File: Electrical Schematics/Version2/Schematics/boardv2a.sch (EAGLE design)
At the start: 562 parts, among them IC1 MCP41HVX1ST, IC2 ADUM4160BRW, IC3 SE555D, IC4 4030D, IC5 74LVC1G04DBV, IC6 74LVC1G04DBV, IC7 4030D, K1 G5V-2, Q1 IRLML2060TRPBFBSS123LT1G, Q10 IRLML2060TRPBFBSS123LT1G, Q11 IRLML2060TRPBFBSS123LT1G, Q13 IRLML2060TRPBFBSS123LT1G, Q14 IRLML2060TRPBFBSS123LT1G, Q15 IRLML2060TRPBFBSS123LT1G, Q16 IRLML2060TRPBFBSS123LT1G, Q17 IRLML2060TRPBFBSS123LT1G, Q18 BSP170P, Q19 IRLML2060TRPBFBSS123LT1G, Q2 IRLML2060TRPBFBSS123LT1G, Q3 IRLML2060TRPBFBSS123LT1G, Q4 BSP170P, Q5 IRLML2060TRPBFBSS123LT1G, Q6 IRLML2060TRPBFBSS123LT1G, Q7 ASFL1, Q8 IRLML2060TRPBFBSS123LT1G, Q9 IRLML2060TRPBFBSS123LT1G, U1 CP2130-GM, U10 SN65HVDA100-Q1_D_8, U11 ADUM3442CRWZ, U12 ADUM3442CRWZ, U13 ADUM3442CRWZ, U14 ADUM3442CRWZ, U15 ADUM3442CRWZ, U16 ADUM3442CRWZ, U17 ADUM3442CRWZ, U18 LM1085_KTT_3, U19 ADUM3442CRWZ, U2 TMS570LS0432_PZ_100, U20 ADUM3442CRWZ, U3 LM1085_KTT_3, U4 LM1085_KTT_3, U5 LM1084_KTT_3, U6 TPS3514_D_14, U7 LM1085_KTT_3, U9 ADUM3442CRWZ, X4 5566-4

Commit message: updarted board
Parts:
- removed IC4: 4030D, 40xx:4030D
- removed JP50: (no value), jumper:JP1Q
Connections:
- removed net CON_MOND_+: JP85.2
- removed net CON_MOND_-: C57.2
- removed net N$63: JP27.1
- new net FNR_CON_FD: D1.C, Q19.D, R14.2, TP149.TP
- new net FNR_CON_RD: D2.C, Q2.S, R15.2, TP148.TP
- net 5V_FNR: now also IC3.V+, IC7P.VDD, TP158.TP; no longer IC4P.VDD
- net CON_FNR_POTGND: now also TP160.TP
- net CON_MONA_+: now also JP85.2
- net CON_MONA_-: now also C57.2
- net CON_MONB_-: now also IC7P.VSS, TP159.TP; no longer IC4P.VSS
- net CON_RIN: now also JP27.1
- net FNR_CON_F: no longer D2.C, Q2.S, R15.2
- net FNR_CON_R: no longer D1.C, Q19.D, R14.2, TP149.TP
- net N$59: now also IC3.DIS
- net N$61: now also IC3.TR
- net N$62: now also IC3.Q
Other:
- moved on the sheet: C57, D1, JP27, JP85, PTC1, Q4, TP148, TP158, TP159, TP160

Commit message: updated stuff
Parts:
- removed TP143: TPB1,27, testpad:TPB1,27
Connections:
- new net 5V_SUP_J1: JP23.2, U$2.VSUP
- net 5V_SUPERVISED: no longer JP23.2, U$2.VSUP
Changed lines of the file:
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@@
 <part name="D3" library="diode" deviceset="GF1" device=""/>
 <part name="IC7" library="40xx" deviceset="4030" device="D"/>
-<part name="TP143" library="testpad" deviceset="TP" device="B1,27"/>
 <part name="TP144" library="testpad" deviceset="TP" device="B1,27"/>
 <part name="TP145" library="testpad" deviceset="TP" device="B1,27"/>
@@
 <net name="5V_SUPERVISED" class="0">
 <segment>
-<wire x1="50.8" y1="85.09" x2="52.07" y2="85.09" width="0.1524" layer="91"/>
-<wire x1="52.07" y1="85.09" x2="90.17" y2="85.09" width="0.1524" layer="91"/>
-<pinref part="U$2" gate="A" pin="VSUP"/>
-<junction x="52.07" y="85.09"/>
-<pinref part="JP23" gate="A" pin="2"/>
-<wire x1="90.17" y1="85.09" x2="90.17" y2="82.55" width="0.1524" layer="91"/>
-</segment>
-<segment>
 <pinref part="C9" gate="G$1" pin="1"/>
 <wire x1="97.79" y1="81.28" x2="110.49" y2="81.28" width="0.1524" layer="91"/>
@@
 </segment>
 </net>
+<net name="5V_SUP_J1" class="0">
+<segment>
+<wire x1="50.8" y1="85.09" x2="52.07" y2="85.09" width="0.1524" layer="91"/>
+<wire x1="52.07" y1="85.09" x2="90.17" y2="85.09" width="0.1524" layer="91"/>
+<pinref part="U$2" gate="A" pin="VSUP"/>
+<junction x="52.07" y="85.09"/>
+<pinref part="JP23" gate="A" pin="2"/>
+<wire x1="90.17" y1="85.09" x2="90.17" y2="82.55" width="0.1524" layer="91"/>
+</segment>
+</net>
 </nets>
 </sheet>
@@
 <instance part="IC5" gate="P" x="-71.12" y="22.86"/>
 <instance part="IC6" gate="P" x="-78.74" y="22.86"/>
-<instance part="TP143" gate="G$1" x="-17.78" y="76.2"/>
 <instance part="TP144" gate="G$1" x="-7.62" y="74.93"/>
 <instance part="TP145" gate="G$1" x="6.35" y="38.1"/>
@@
 <segment>
 <pinref part="D2" gate="D" pin="A"/>
-<label x="138.43" y="-41.91" size="1.778" layer="95" xref="yes"/>
-<wire x1="138.43" y1="-41.91" x2="119.38" y2="-40.64" width="0.1524" layer="91"/>
-<wire x1="137.16" y1="-36.83" x2="138.43" y2="-41.91" width="0.1524" layer="91"/>
+<label x="137.16" y="-40.64" size="1.778" layer="95" xref="yes"/>
+<wire x1="137.16" y1="-40.64" x2="119.38" y2="-40.64" width="0.1524" layer="91"/>
+<wire x1="137.16" y1="-36.83" x2="137.16" y2="-40.64" width="0.1524" layer="91"/>
 <pinref part="JP27" gate="A" pin="2"/>
 <wire x1="129.54" y1="-36.83" x2="137.16" y2="-36.83" width="0.1524" layer="91"/>
@@
 <junction x="41.91" y="76.2"/>
 </segment>
-<segment>
-<wire x1="39.37" y1="78.74" x2="40.64" y2="78.74" width="0.1524" layer="91"/>
-</segment>
 </net>

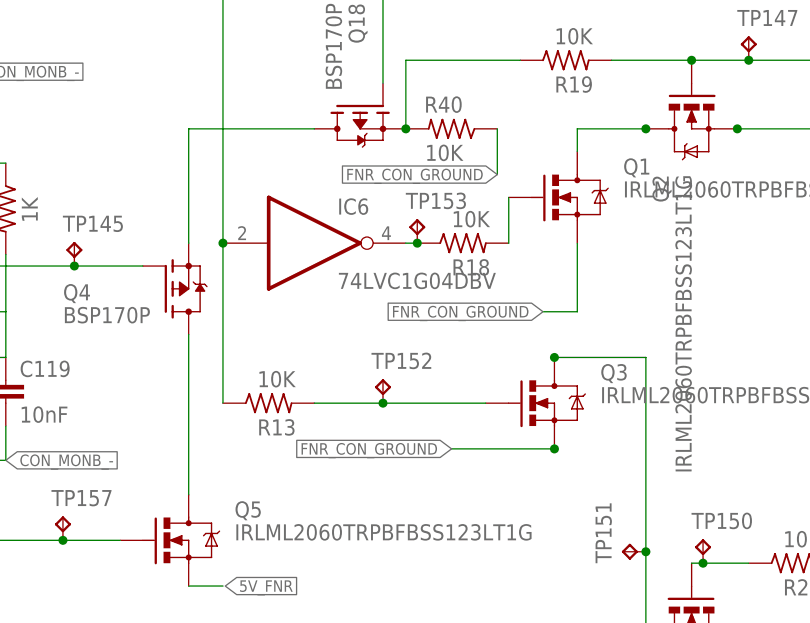
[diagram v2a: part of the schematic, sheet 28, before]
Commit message: fixed FNR ground
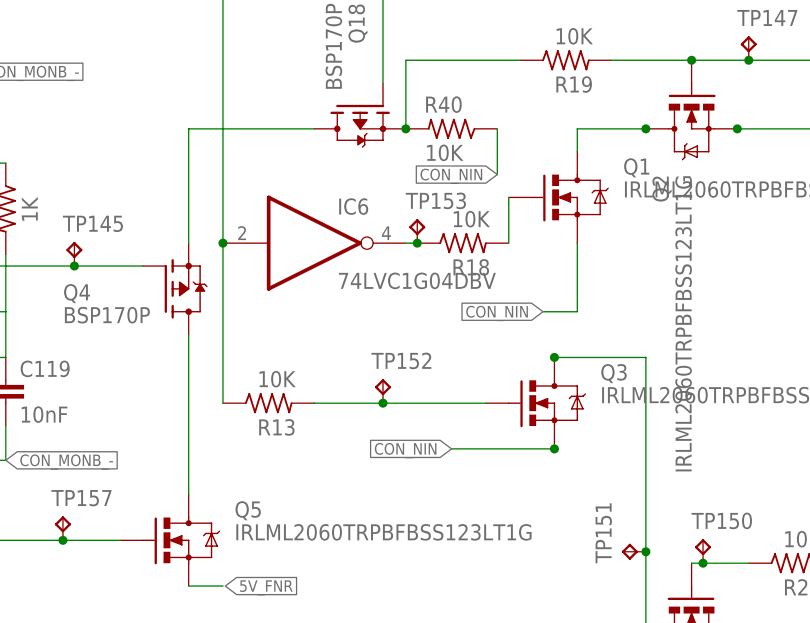
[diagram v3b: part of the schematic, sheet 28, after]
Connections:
- net CON_NIN: now also Q1.S, Q3.S, R40.1
- net FNR_CON_GROUND: no longer Q1.S, Q3.S, R40.1
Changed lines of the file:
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@@
 <setting verticaltext="up"/>
 </settings>
-<grid distance="0.05" unitdist="inch" unit="inch" style="lines" multiple="1" display="no" altdistance="0.025" altunitdist="inch" altunit="inch"/>
+<grid distance="0.1" unitdist="inch" unit="inch" style="lines" multiple="1" display="no" altdistance="0.01" altunitdist="inch" altunit="inch"/>
 <layers>
 <layer number="1" name="Top" color="4" fill="1" visible="no" active="no"/>
@@
 </segment>
 </net>
-<net name="FNR_CON_GROUND" class="0">
-<segment>
-<pinref part="Q3" gate="G$1" pin="S"/>
-<label x="48.26" y="15.24" size="1.27" layer="95" rot="R180" xref="yes"/>
-<wire x1="59.69" y1="15.24" x2="48.26" y2="15.24" width="0.1524" layer="91"/>
-<junction x="59.69" y="15.24"/>
-</segment>
-<segment>
-<wire x1="62.23" y1="38.1" x2="62.23" y2="30.48" width="0.1524" layer="91"/>
-<wire x1="62.23" y1="30.48" x2="58.42" y2="30.48" width="0.1524" layer="91"/>
-<label x="58.42" y="30.48" size="1.27" layer="95" rot="R180" xref="yes"/>
-<pinref part="Q1" gate="G$1" pin="S"/>
-</segment>
-<segment>
-<pinref part="R40" gate="G$1" pin="1"/>
-<wire x1="53.34" y1="50.8" x2="53.34" y2="45.72" width="0.1524" layer="91"/>
-<label x="53.34" y="45.72" size="1.27" layer="95" rot="R180" xref="yes"/>
-</segment>
-</net>
 <net name="FNR_CON_R" class="0">
 <segment>
@@
 <junction x="41.91" y="76.2"/>
 </segment>
+<segment>
+<pinref part="R40" gate="G$1" pin="1"/>
+<wire x1="53.34" y1="50.8" x2="53.34" y2="45.72" width="0.1524" layer="91"/>
+<label x="53.34" y="45.72" size="1.27" layer="95" rot="R180" xref="yes"/>
+</segment>
+<segment>
+<pinref part="Q3" gate="G$1" pin="S"/>
+<label x="48.26" y="15.24" size="1.27" layer="95" rot="R180" xref="yes"/>
+<wire x1="59.69" y1="15.24" x2="48.26" y2="15.24" width="0.1524" layer="91"/>
+<junction x="59.69" y="15.24"/>
+</segment>
+<segment>
+<wire x1="62.23" y1="38.1" x2="62.23" y2="30.48" width="0.1524" layer="91"/>
+<wire x1="62.23" y1="30.48" x2="58.42" y2="30.48" width="0.1524" layer="91"/>
+<label x="58.42" y="30.48" size="1.27" layer="95" rot="R180" xref="yes"/>
+<pinref part="Q1" gate="G$1" pin="S"/>
+</segment>
 </net>

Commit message: did some lagit routing
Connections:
- net MCU_COMMS_MISO: now also JP14.1
- net MCU_COMMS_SCK: now also JP18.2
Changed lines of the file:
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@@
 <junction x="114.3" y="-7.62"/>
 <wire x1="355.6" y1="-93.98" x2="355.6" y2="-86.36" width="0.1524" layer="91"/>
-<wire x1="355.6" y1="-86.36" x2="373.38" y2="-86.36" width="0.1524" layer="91"/>
+<wire x1="355.6" y1="-86.36" x2="370.84" y2="-86.36" width="0.1524" layer="91"/>
 <pinref part="JP13" gate="A" pin="2"/>
+<wire x1="370.84" y1="-86.36" x2="373.38" y2="-86.36" width="0.1524" layer="91"/>
 <wire x1="355.6" y1="-93.98" x2="375.92" y2="-93.98" width="0.1524" layer="91"/>
 <junction x="355.6" y="-93.98"/>
+<pinref part="JP14" gate="A" pin="1"/>
+<junction x="370.84" y="-86.36"/>
 </segment>
 </net>
@@
 <wire x1="375.92" y1="-116.84" x2="370.84" y2="-116.84" width="0.1524" layer="91"/>
 <wire x1="370.84" y1="-116.84" x2="370.84" y2="-121.92" width="0.1524" layer="91"/>
-<wire x1="370.84" y1="-121.92" x2="378.46" y2="-121.92" width="0.1524" layer="91"/>
+<wire x1="370.84" y1="-121.92" x2="375.92" y2="-121.92" width="0.1524" layer="91"/>
 <junction x="370.84" y="-116.84"/>
+<pinref part="JP18" gate="A" pin="2"/>
+<wire x1="375.92" y1="-121.92" x2="378.46" y2="-121.92" width="0.1524" layer="91"/>
+<junction x="375.92" y="-121.92"/>
 </segment>
 </net>

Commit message: Lots of routing and some lib updates
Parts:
- removed R22, R23: (no value), resistor-bourns:4816P-T01E
- removed TP117: TPB1,27, testpad:TPB1,27
- added U$32, U$4: RHM1620CT-ND, shit:RHM1620CT-ND
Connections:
- new net 5V_SU_J: JP25.2, U$3.VSUP
- new net N$301: JP80.8
- new net N$302: JP80.7
- net 5V_SUPERVISED: no longer JP25.2, U$3.VSUP
- net FPGA_MCU_AD1: now also U$4G$7.P$1; no longer R22B.1
- net FPGA_MCU_AD2: now also U$4G$6.P$1; no longer R22C.1
- net FPGA_MCU_AD3: now also U$4G$5.P$1; no longer R22D.1
- net FPGA_MCU_AD4: now also U$4G$4.P$1; no longer R22E.1
- net FPGA_MCU_AD5: now also U$4G$3.P$1; no longer R22F.1
- net FPGA_MCU_AD6: now also U$4G$2.P$1; no longer R22G.1
- net FPGA_MCU_AD7: now also U$4G$1.P$1; no longer R22H.1
- net FPGA_MCU_AD7_RES: now also U$4G$1.P$2; no longer R22H.2
- net FPGA_MCU_ADO: now also U$4G$8.P$1; no longer R22A.1
- net FPGA_MCU_RES1: now also U$32G$1.P$1; no longer R23A.1
- net FPGA_MCU_RES1_RES: now also U$32G$1.P$2; no longer R23A.2
- net FPGA_MCU_RES2: now also U$32G$2.P$1; no longer R23B.1
- net FPGA_MCU_RES2_RES: now also U$32G$2.P$2; no longer R23B.2
- net FPGA_MCU_RES3: now also U$32G$3.P$1; no longer R23C.1
- net FPGA_MCU_RES3_RES: now also U$32G$3.P$2; no longer R23C.2
- net FPGA_MCU_RES4: now also U$32G$4.P$1; no longer R23D.1
- net FPGA_MCU_RES4_RES: now also U$32G$4.P$2; no longer R23D.2
- net GND: now also L7.1
- net MCU_IO_RALAYB: now also U$2.PA4
- net N$185: no longer TP117.TP
- net N$34: now also U$4G$8.P$2; no longer R22A.2
- net N$35: now also U$4G$7.P$2; no longer R22B.2
- net N$36: now also U$4G$6.P$2; no longer R22C.2
- net N$39: now also U$4G$5.P$2; no longer R22D.2
- net N$52: now also U$4G$4.P$2; no longer R22E.2
- net N$53: now also U$4G$3.P$2; no longer R22F.2
- net N$54: now also U$4G$2.P$2; no longer R22G.2
- net N$87: no longer JP80.7
- net N$88: no longer JP80.8
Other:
- moved on the sheet: L7, TP61

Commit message: cleaned up FPGA
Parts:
- removed JP75, JP79, JP80, JP89, JP90, JP91, JP92, JP93, JP94, JP95: (no value), pinhead:PINHD-1X8
- added TP117, TP143, TP165, TP166, TP167, TP168, TP169, TP170, TP171, TP172, TP173, TP174, TP175, TP176, TP177, TP178, TP179, TP180, TP181, TP182, TP183, TP184, TP185, TP186, TP187, TP188, TP189, TP190, TP191, TP192, TP193, TP194, TP195, TP196, TP197, TP198, TP199, TP200, TP201, TP202, TP203, TP204, TP205, TP206, TP207, TP208, TP209, TP210, TP211, TP212, TP213, TP214, TP215, TP216, TP217, TP218, TP219, TP220, TP221, TP222, TP223, TP224, TP225, TP228, TP229, TP230, TP231, TP232, TP233: TPPAD1-13, testpad:TPPAD1-13
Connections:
- removed net N$301: JP80.8
- removed net N$302: JP80.7
- removed net NC: JP90.7
- net FPGA_L12N_2: now also TP185.TP; no longer JP90.2
- net FPGA_L12P_2: now also TP186.TP; no longer JP90.1
- net FPGA_L13N_2: now also TP183.TP; no longer JP90.4
- net FPGA_L13P_2: now also TP184.TP; no longer JP90.3
- net FPGA_L14N_2: now also TP181.TP; no longer JP90.6
- net FPGA_L14P_2: now also TP182.TP; no longer JP90.5
- net FPGA_L1N_0: now also TP204.TP; no longer JP94.2
- net FPGA_L1N_1: no longer JP95.4
- net FPGA_L1N_2: now also TP174.TP; no longer JP91.4
- net FPGA_L1N_3: now also TP215.TP; no longer JP93.6
- net FPGA_L1P_0: now also TP203.TP; no longer JP94.1
- net FPGA_L1P_1: no longer JP95.3
- net FPGA_L1P_2: now also TP176.TP; no longer JP91.3
- net FPGA_L1P_3: now also TP214.TP; no longer JP93.5
- net FPGA_L2N_0: now also TP206.TP; no longer JP94.4
- net FPGA_L2N_2: now also TP173.TP; no longer JP91.6
- net FPGA_L2N_3: now also TP217.TP; no longer JP93.8
- net FPGA_L2P_0: now also TP205.TP; no longer JP94.3
- net FPGA_L2P_2: now also TP175.TP; no longer JP91.5
- net FPGA_L2P_3: now also TP216.TP; no longer JP93.7
- net FPGA_L30N_2: now also TP179.TP; no longer JP90.8
- net FPGA_L31N_2: now also TP193.TP; no longer JP89.2
- net FPGA_L31P_2: now also TP194.TP; no longer JP89.1
- net FPGA_L32N_1: no longer JP95.6
- net FPGA_L32P_1: no longer JP95.5
- net FPGA_L36N_3: now also TP231.TP; no longer JP80.2
- net FPGA_L36P_3: now also TP233.TP; no longer JP80.1
- net FPGA_L37N_3: now also TP230.TP; no longer JP80.4
- net FPGA_L37P_3: now also TP232.TP; no longer JP80.3
- net FPGA_L3N_0: now also TP209.TP; no longer JP94.6
- net FPGA_L3N_2: now also TP117.TP; no longer JP91.8
- net FPGA_L3P_0: now also TP207.TP; no longer JP94.5
- net FPGA_L3P_2: now also TP172.TP; no longer JP91.7
- net FPGA_L41N_3: now also TP228.TP; no longer JP80.6
- net FPGA_L41P_3: now also TP229.TP; no longer JP80.5
- net FPGA_L42N_3: now also TP224.TP; no longer JP79.2
- net FPGA_L42N_GCLK6_TRDY1_1: no longer JP95.8
- net FPGA_L42P_1: no longer JP95.7
- net FPGA_L42P_3: now also TP225.TP; no longer JP79.1
- net FPGA_L43N_1: now also TP169.TP; no longer JP92.2
- net FPGA_L43N_3: now also TP222.TP; no longer JP79.4
- net FPGA_L43P_1: now also TP170.TP; no longer JP92.1
- net FPGA_L43P_3: now also TP223.TP; no longer JP79.3
- net FPGA_L44N_3: now also TP220.TP; no longer JP79.6
- net FPGA_L44P_3: now also TP221.TP; no longer JP79.5
- net FPGA_L45N_1: now also TP167.TP; no longer JP92.4
- net FPGA_L45P_1: now also TP168.TP; no longer JP92.3
- net FPGA_L46N_1: now also TP165.TP; no longer JP92.6
- net FPGA_L46P_1: now also TP166.TP; no longer JP92.5
- net FPGA_L47N_1: now also TP171.TP; no longer JP92.8
- net FPGA_L47P_1: now also TP143.TP; no longer JP92.7
- net FPGA_L48N_2: now also TP191.TP; no longer JP89.4
- net FPGA_L48P_2: now also TP192.TP; no longer JP89.3
- net FPGA_L49N_2: now also TP189.TP; no longer JP89.6
- net FPGA_L49P_2: now also TP190.TP; no longer JP89.5
- net FPGA_L4N_0: now also TP208.TP; no longer JP94.8
- net FPGA_L4P_0: now also TP180.TP; no longer JP94.7
- net FPGA_L62N_0: now also TP201.TP; no longer JP75.2
- net FPGA_L62N_2: now also TP187.TP; no longer JP89.8
- net FPGA_L62P_0: now also TP202.TP; no longer JP75.1
- net FPGA_L62P_2: now also TP188.TP; no longer JP89.7
- net FPGA_L63N_0: now also TP199.TP; no longer JP75.4
- net FPGA_L63P_0: now also TP200.TP; no longer JP75.3
- net FPGA_L64N_0: now also TP197.TP; no longer JP75.6
- net FPGA_L64N_2: now also TP211.TP; no longer JP93.2
- net FPGA_L64P_0: now also TP198.TP; no longer JP75.5
- net FPGA_L64P_2: now also TP210.TP; no longer JP93.1
- net FPGA_L65N_0: now also TP195.TP; no longer JP75.8
- net FPGA_L65N_2: now also TP213.TP; no longer JP93.4
- net FPGA_L65P_0: now also TP196.TP; no longer JP75.7
- net FPGA_L65P_2: now also TP212.TP; no longer JP93.3
- net FPGA_L66N_0: no longer JP95.2
- net FPGA_L66P_0: no longer JP95.1
- net FPGA_L74N_1: now also TP177.TP; no longer JP91.2
- net FPGA_L74P_1: now also TP178.TP; no longer JP91.1
- net FPGA_L83N_3: now also TP218.TP; no longer JP79.8
- net FPGA_L83P_3: now also TP219.TP; no longer JP79.7

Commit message: Fix a bunch
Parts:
- removed LED25: (no value), eagle-ltspice:LED_E
- removed Q14, Q15, Q16: IRLML2060TRPBFBSS123LT1G, SparkFun-DiscreteSemi:IRLML2060TRPBFBSS123LT1G
- removed R100, R101, R102: .01, SparkFun-Passives:RESISTOR0603-RES
- removed R34: 600, SparkFun-Passives:RESISTOR0603-RES
- removed TP150: TPB1,27, testpad:TPB1,27
- added C16: 0.1uF, eagle-ltspice:CC0603
- added JP28, JP29, JP30: (no value), jumper:JP1E
- added K2: CP1SA-12V, relay:CP1SA-12V
- added Q12: IRLML2060TRPBFBSS123LT1G, SparkFun-DiscreteSemi:IRLML2060TRPBFBSS123LT1G
- added R12, R22, R23: 3.3k, SparkFun-Passives:RESISTOR0603-RES
- added R29: (no value), SparkFun-Passives:RESISTOR0603-RES
- added R30: 10k, SparkFun-Passives:RESISTOR0603-RES
- added SV3, SV4, SV5: (no value), con-lstb:MA03-2
- Q18, Q4: value BSP170P -> MOSFET-PCHANNEL; device transistor-fet:BSP170P -> SparkFun-DiscreteSemi:MOSFET-PCHANNEL
- Q5: value IRLML2060TRPBFBSS123LT1G -> MOSFET-PCHANNEL; device SparkFun-DiscreteSemi:IRLML2060TRPBFBSS123LT1G -> SparkFun-DiscreteSemi:MOSFET-PCHANNEL
- TP133, TP134, TP135, TP136, TP137, TP138, TP139, TP140: value TPB2,54 -> TPPAD1-13; device testpad:TPB2,54 -> testpad:TPPAD1-13
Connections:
- removed net N$12: LED25.A, TP36.TP, U2.CAN1TX
- removed net N$124: U$3.*RESET, U$3.*RESET_A
- removed net N$128: C13.1, U$3.VDDD2D, U$3.VDDH
- removed net N$137: Q2.G, R19.2, R20.2, TP147.TP
- removed net N$163: JP49.2, Q14.S
- removed net N$23: LED25.C, R34.2
- removed net N$235: JP51.2, Q15.S
- removed net N$236: JP52.2, Q16.S
- removed net N$238: Q15.G, R101.2
- removed net N$239: Q16.G, R100.2
- removed net N$243: Q14.G, R102.2
- new net BKGND: R12.1, SV3.6, U$1.BKGD/MODC
- new net BKGNDB: R22.1, SV4.6
- new net BKGNDC: R23.1, SV5.6
- new net ETHERNET_MCU_INT: R30.2, TP51.TP, U2.GIOA[3]/INT[3], U8.*INT
- new net N$19: JP30.1, U$3.*RESET_A
- new net N$20: JP85.1, K22.P
- new net N$21: JP28.1, U$1.*RESET_A
- new net N$63: K21.1, Q12.S
- new net N$9: JP29.1, U$2.*RESET_A
- new net POWER_GOOD_OUTD: Q12.G, R29.1
- new net USBSPI_MCU_RTR: TP36.TP, U1.GPIO.3/*CS3/RTR, U2.CAN1TX
- new net VDDX: C2.1, R12.2, SV3.1, U$1.VDDRX, U$1.VDDX
- new net VDDXB: C7.1, R22.2, SV4.1, U$2.VDDRX, U$2.VDDX
- new net VDDXC: C13.1, R23.2, SV5.1, U$3.VDDD2D, U$3.VDDH
- new net VSUP: JP21.2, U$1.VSUP
- net 12V_SUPERVISED: now also U$5.P$19
- net 12V_SUPERVISEDB: now also JP49.2; no longer Q14.D
- net 3.3V_SUPERVISEDB: now also JP52.2; no longer Q16.D
- net 5V_FNR: now also Q5.D; no longer Q5.S
- net 5V_SUPERVISED: no longer JP21.2, U$1.VSUP
- net 5V_SUPERVISEDB: now also JP51.2; no longer Q15.D
- net CON_FNR_HIGH: now also U$5.P$18; no longer U$5.P$19
- net CON_MONB_-: now also Q6.S; no longer Q6.D
- net CON_NIN: now also U$5.P$15; no longer U$5.P$20
- net ETHERNET_3.3_J_+: now also C16.1, U$22.R3
- net FNR_CON_RD: now also Q2.D; no longer Q2.S
- net FPGA_MCU_RES: no longer TP51.TP, U2.GIOA[3]/INT[3]
- net GND: now also C16.2, Q12.D, R30.1, SV3.5, SV4.5, SV5.5, U$5.P$20; no longer R34.1
- net MCU_FNR_ENABLEO: now also R20.1; no longer Q5.G
- net N$130: now also Q5.S; no longer Q5.D
- net N$139: now also Q2.S; no longer Q2.D
- net N$14: now also JP28.2, SV3.3; no longer U$1.*RESET_A
- net N$142: now also Q2.G, R19.2, TP147.TP; no longer R20.1, TP150.TP
- net N$2: now also JP30.2, SV5.3, U$3.*RESET; no longer C2.1, U$1.VDDRX, U$1.VDDX
- net N$33: now also Q5.G, R20.2; no longer C7.1, U$2.VDDRX, U$2.VDDX
- net N$40: now also JP29.2, SV4.3; no longer U$2.*RESET_A
- net N$57: now also Q6.D; no longer Q6.S
- net POWER_GOOD_OUT: now also R29.2; no longer R100.1, R101.1, R102.1
- net SPIBRIDGE_3.3V: now also U1.VIO
- net VOLTAGEJMP_+_TO_INPUT_VREG: no longer JP85.1, JP96.2
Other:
- moved on the sheet: JP85, Q17, Q2, Q5, Q6, R17, R20, TP157
